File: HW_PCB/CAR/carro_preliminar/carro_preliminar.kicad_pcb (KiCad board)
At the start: 2 copper layers, 25 parts, among them J1 V_Battery, J2 STLINK, J3 Puente H, J4 Puente_H2, J5 UART, J6 Servo_Motor, J7 NRF24_Con, SW1 SW_DPST_x2, U1 STM32F103C8Tx, U2 AMS1117-3.3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

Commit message: Carrito pcb, 25-02-26
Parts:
- removed J4: Puente_H2, Connector_PinHeader_2.54mm:PinHeader_1x08_P2.54mm_Vertical
- added C10: 100nF, Capacitor_SMD:C_0805_2012Metric_Pad1.18x1.45mm_HandSolder, B.Cu at (162.1, 83.2)
- added C11: 10uF, Capacitor_SMD:C_0805_2012Metric_Pad1.18x1.45mm_HandSolder, B.Cu at (193.0, 83.7)
- added C12: 100nF, Capacitor_SMD:C_0805_2012Metric_Pad1.18x1.45mm_HandSolder, B.Cu at (183.1, 84.5)
- added C13: 10uF, Capacitor_SMD:C_0805_2012Metric_Pad1.18x1.45mm_HandSolder, F.Cu at (190.0, 97.7)
- added C1_Driver1: 0.1uF, Capacitor_SMD:C_0805_2012Metric, F.Cu at (186.8, 100.2)
- added C2_driver1: 0.1uF, Capacitor_SMD:C_0805_2012Metric, F.Cu at (185.1, 94.6)
- added C3_Driver1: TAJB226K016RNJ_10uF, TAJB226K016RNJ:CAPPC3528X210N, F.Cu at (184.2, 79.0)
- added IC1: TB6612FNG, Package_SO:SSOP-24_5.3x8.2mm_P0.65mm, F.Cu at (177.3, 86.3)
- added U3: AMS1117-3.3, Package_TO_SOT_SMD:SOT-223-3_TabPin2, B.Cu at (152.6, 81.8)
- C2, C3, C4, C5, C6, C7, C8, R1, R2, R3, U2: moved to B.Cu
- J3: value Puente H -> Motores; footprint Connector_PinHeader_2.54mm:PinHeader_1x08_P2.54mm_Vertical -> Connector_PinHeader_2.54mm:PinHeader_1x04_P2.54mm_Vertical
- moved J3 105.4 mm to (188.3, 81.5)
- moved C7 93.6 mm to (182.9, 86.6), turned to 180 degrees
- moved C5 75.6 mm to (162.8, 92.3)
- moved J5 73.2 mm to (170.7, 97.1), turned to 90 degrees
- moved Y1 73.1 mm to (161.7, 98.7), turned to 180 degrees
- moved C6 70.9 mm to (158.7, 92.3), turned to 180 degrees
- moved C9 69.2 mm to (158.2, 94.1)
- moved C8 62.8 mm to (152.1, 88.4), turned to 180 degrees
- moved R3 57.5 mm to (163.8, 79.4)
- moved R1 55.5 mm to (162.3, 87.8)
- moved U1 55.0 mm to (160.2, 86.7)
- moved J2 52.3 mm to (154.5, 73.7)
- moved R2 50.6 mm to (157.6, 88.1), turned to 180 degrees
- moved C2 49.9 mm to (137.7, 77.7), turned to 180 degrees
- moved C3 49.9 mm to (137.7, 80.7), turned to 180 degrees
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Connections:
- J3 pad 1: VM -> /B02
- J3 pad 2: VCC -> /B01
- J3 pad 3: GND -> /A02
- J3 pad 4: A01 -> /A01
- J5 pad 1: Tx -> PB10
- J5 pad 2: Rx -> PB11
- J6 pad 1: PWM -> PB5
- J7 pad 2: CE -> PA10
- J7 pad 3: SCK -> PB13
- J7 pad 4: MISO -> PB14
- J7 pad 5: IRQ -> PA9
- J7 pad 6: MOSI -> PB15
- J7 pad 7: CNS -> PA8
- J7 pad 8: VCC -> VCC_nrf24l01
- R3 pad 1: PC13 -> VCC_nrf24l01
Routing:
- net PB13: track 0.00 -> 40.0 mm
- net PB15: track 0.00 -> 25.2 mm
- net PB14: track 0.00 -> 21.6 mm
- net PA8: track 0.00 -> 18.9 mm
- net PA9: track 0.00 -> 18.5 mm
- net VCC_nrf24l01: track 0.00 -> 18.2 mm
- net SWDIO: track 0.00 -> 3.32 mm
- net SWCLK: track 0.00 -> 0.63 mm

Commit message: Carrito 26-02-26
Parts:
- C1_Driver1, C2_driver1, C3_Driver1, D1: moved to B.Cu
- C7: moved to F.Cu
- moved C11 43.5 mm to (149.8, 78.0), turned to 0 degrees
- moved C13 22.9 mm to (175.1, 80.3), turned to 180 degrees
- moved D1 21.7 mm to (149.9, 80.1), turned to 180 degrees
- moved C1_Driver1 20.9 mm to (196.9, 81.9), turned to -90 degrees
- moved R1 18.2 mm to (156.4, 70.5)
- moved C8 16.6 mm to (136.0, 92.1)
- moved C12 16.1 mm to (188.4, 69.2)
- moved C3_Driver1 15.2 mm to (169.3, 82.1), turned to -90 degrees
- moved C10 14.7 mm to (149.7, 75.3)
- moved R3 14.2 mm to (150.0, 82.8)
- moved J2 10.9 mm to (165.0, 76.5)
- moved C1 9.00 mm to (169.3, 100.2)
- moved R2 8.09 mm to (153.2, 94.9)
- moved U2 7.01 mm to (178.3, 84.3), turned to 90 degrees
- moved C7 6.96 mm to (180.1, 80.2), turned to 0 degrees
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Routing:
- net SWCLK: track 0.63 -> 65.0 mm
- net VCC: track 0.00 -> 31.8 mm, vias 0 -> 1
- net PA10: track 0.00 -> 24.0 mm
- net GND: track 0.00 -> 22.4 mm
- net PA1: track 0.00 -> 18.9 mm
- net PA0: track 0.00 -> 14.5 mm
- net PB14: track 21.6 -> 34.9 mm
- net VCC_nrf24l01: track 18.2 -> 31.1 mm
- net SWDIO: track 3.32 -> 16.0 mm, vias 0 -> 1
- net PB5: track 0.00 -> 11.0 mm
- net PA6: track 0.00 -> 10.7 mm
- net PA5: track 0.00 -> 10.7 mm
- net OSC_IN: track 0.00 -> 9.12 mm
- net NRST: track 0.00 -> 8.54 mm
- net PA9: track 18.5 -> 22.1 mm
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
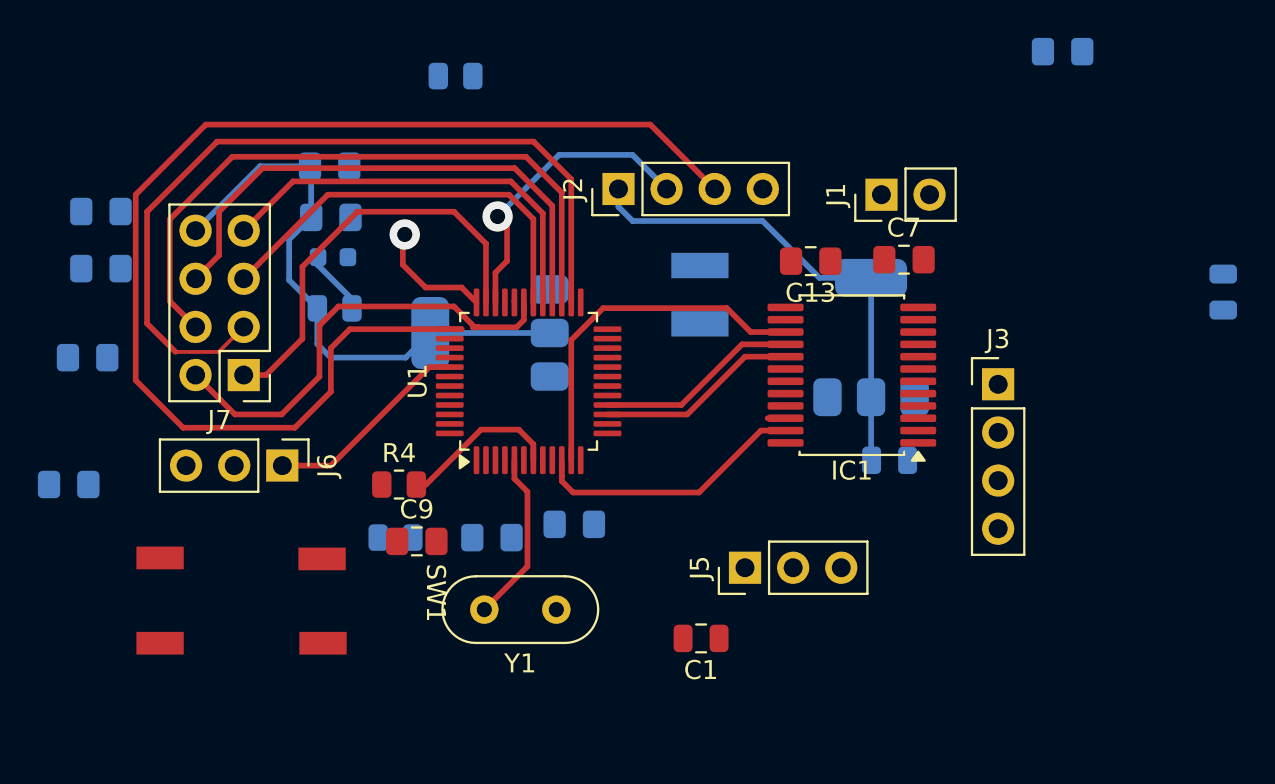
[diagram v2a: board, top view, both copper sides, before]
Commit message: added an advance for the CAR PCB
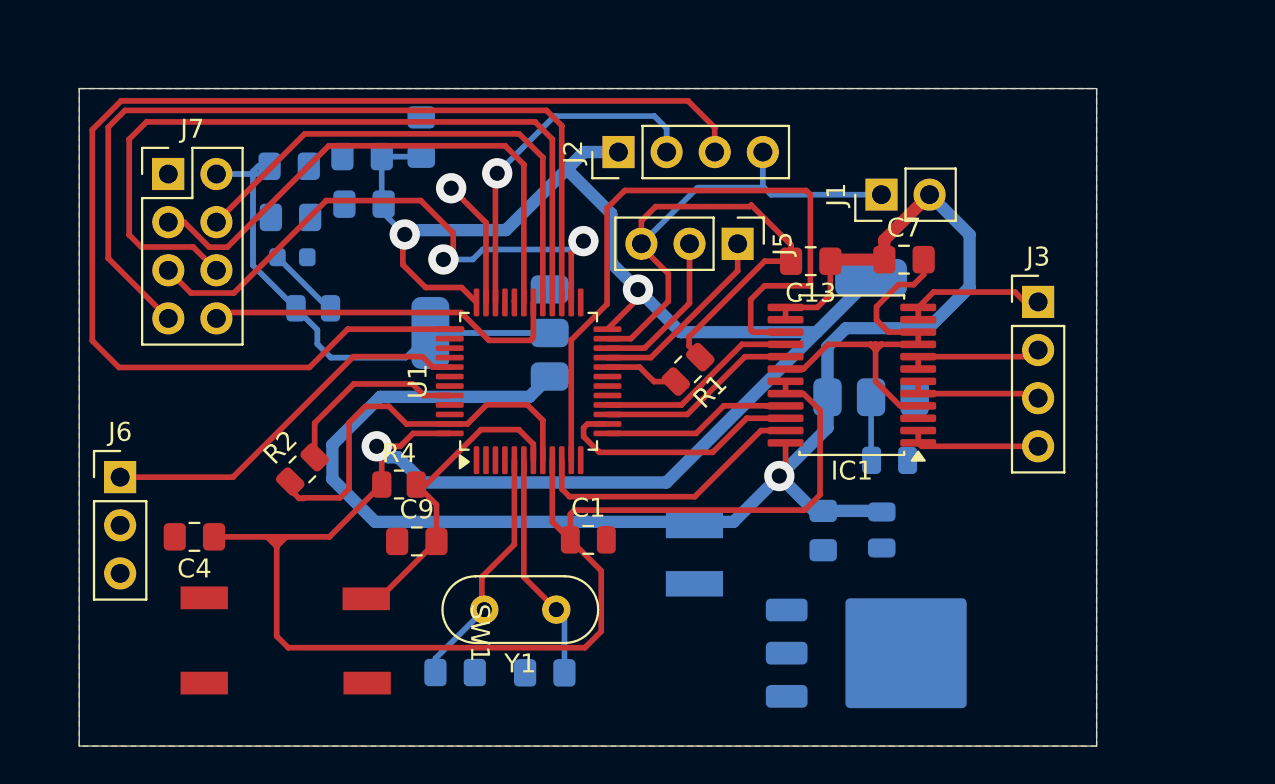
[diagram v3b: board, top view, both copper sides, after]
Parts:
- added U4: LM1117DT-5.0, Package_TO_SOT_SMD:TO-252-3_TabPin2, B.Cu at (178.9, 101.0)
- C4, R1, R2: moved to F.Cu
- J7: value NRF24_Con -> Conn_02x04_Odd_Even
- moved C12 28.3 mm to (175.8, 94.5), turned to -90 degrees
- moved C1_Driver1 22.0 mm to (178.9, 94.5)
- moved C8 21.5 mm to (151.6, 77.3)
- moved R1 19.8 mm to (168.7, 86.0), turned to -135 degrees
- moved C3 18.3 mm to (154.6, 73.8), turned to 90 degrees
- moved J5 17.1 mm to (171.3, 79.4), turned to -90 degrees
- moved C2 14.1 mm to (151.4, 74.8)
- moved C3_Driver1 13.7 mm to (169.0, 95.8), turned to 90 degrees
- moved J7 11.3 mm to (141.2, 75.7), turned to 0 degrees
- moved C4 11.0 mm to (142.6, 94.9)
- moved C5 10.0 mm to (156.4, 102.0)
- moved J6 8.58 mm to (138.7, 91.7), turned to 0 degrees
- moved C1 7.90 mm to (163.4, 95.0), turned to 0 degrees
- moved C6 7.67 mm to (161.1, 102.0)
- moved R2 6.09 mm to (148.3, 91.3), turned to 45 degrees
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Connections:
- J7 pad 2: PA10 -> VCC_nrf24l01
- J7 pad 3: PB13 -> PA10
- J7 pad 4: PB14 -> PA8
- J7 pad 5: PA9 -> PB13
- J7 pad 7: PA8 -> PB14
- J7 pad 8: VCC_nrf24l01 -> PA9
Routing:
- net VCC: track 31.8 -> 159.7 mm, vias 1 -> 3
- net VIN: track 0.00 -> 83.2 mm, vias 0 -> 1
- net GND: track 22.4 -> 92.0 mm, vias 0 -> 1
- net PA1: track 18.9 -> 37.0 mm
- net PB15: track 28.5 -> 42.1 mm
- net PA4: track 0.95 -> 13.6 mm
- net PB13: track 43.4 -> 31.3 mm, vias 0 -> 2
- net OSC_OUT: track 0.00 -> 12.1 mm
- net PB14: track 34.9 -> 45.4 mm
- net PB10: track 0.00 -> 10.2 mm
- net Net-(U1-BOOT0): track 0.00 -> 10.0 mm
- net PA3: track 0.00 -> 10.0 mm
- net PB5: track 11.0 -> 20.3 mm
- net PB11: track 0.00 -> 8.45 mm
- net NRST: track 8.54 -> 16.9 mm
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- added copper zone on B.Cu, net GND
- added copper zone on F.Cu, net GND
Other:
- board outline added: 53.7 x 34.7 mm

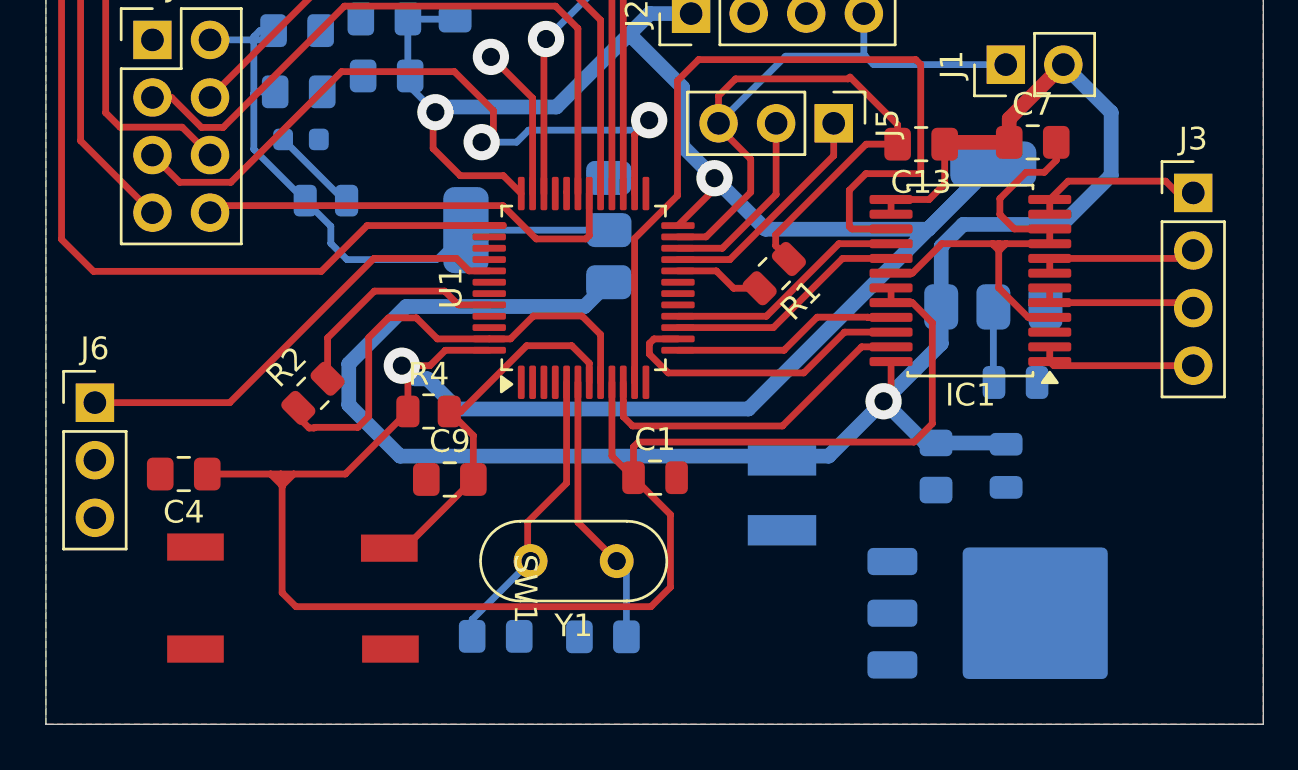
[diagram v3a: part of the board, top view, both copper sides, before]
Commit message: Placa de carro terminada al menos preliminarmente
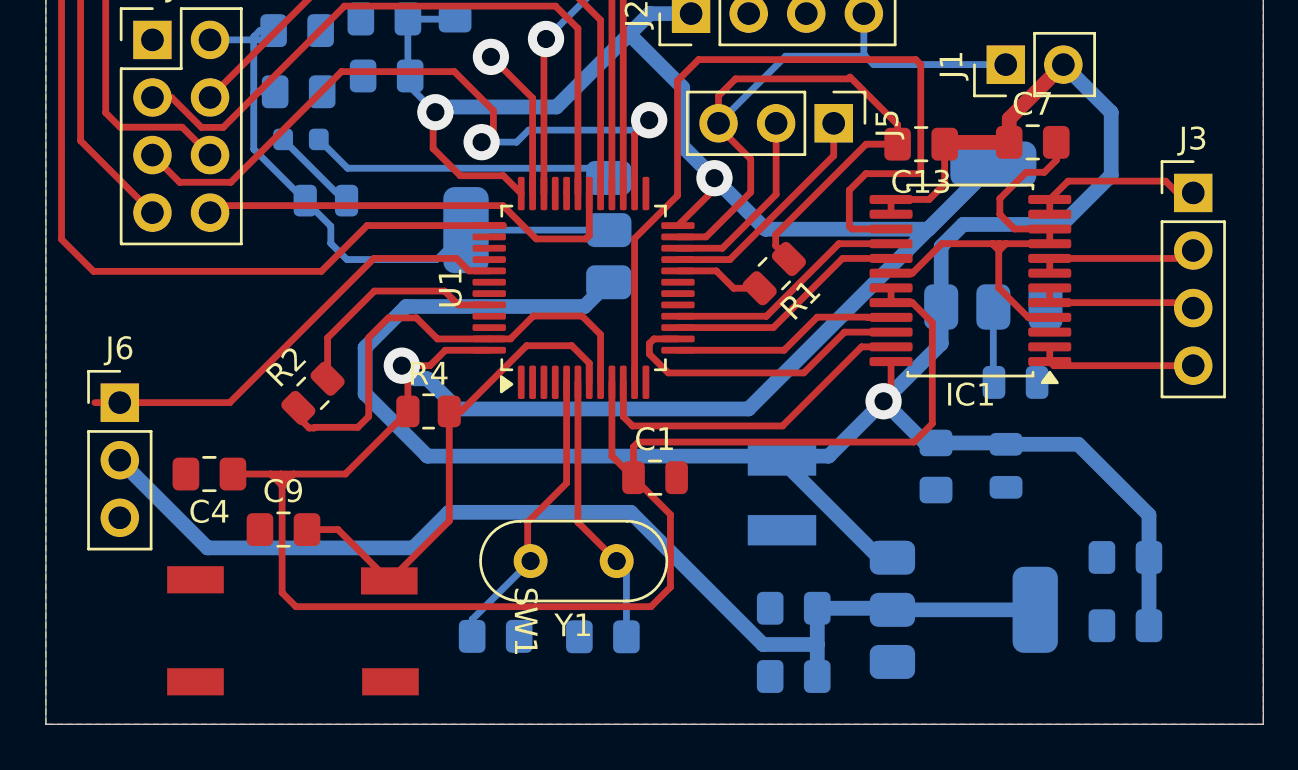
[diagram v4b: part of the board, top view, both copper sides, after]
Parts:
- removed U4: LM1117DT-5.0, Package_TO_SOT_SMD:TO-252-3_TabPin2
- added C14: 10uF, Capacitor_SMD:C_0805_2012Metric_Pad1.18x1.45mm_HandSolder, B.Cu at (184.1, 98.5)
- added C15: 100nF, Capacitor_SMD:C_0805_2012Metric_Pad1.18x1.45mm_HandSolder, B.Cu at (184.1, 101.5)
- added C16: 100nF, Capacitor_SMD:C_0805_2012Metric_Pad1.18x1.45mm_HandSolder, B.Cu at (169.5, 100.8)
- added C17: 100nF, Capacitor_SMD:C_0805_2012Metric_Pad1.18x1.45mm_HandSolder, B.Cu at (169.5, 103.8)
- added U5: AMS1117-5.0, Package_TO_SOT_SMD:SOT-223-3_TabPin2, B.Cu at (177.0, 100.8)
- moved C9 7.66 mm to (147.0, 97.3)
- moved SW1 1.44 mm to (157.2, 101.4)
- moved C4 1.13 mm to (143.7, 94.9)
- moved J6 1.10 mm to (139.8, 91.7)
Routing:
- net 5V: track 0.00 -> 48.1 mm
- net VIN: track 83.2 -> 101.0 mm
- net GND: track 92.0 -> 105.5 mm
- net NRST: track 16.9 -> 21.7 mm
- net VCC: track 159.7 -> 158.6 mm
